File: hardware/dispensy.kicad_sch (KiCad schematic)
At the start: 16 parts, among them U1 DBT50G-7_62-4P, U2 USB-A

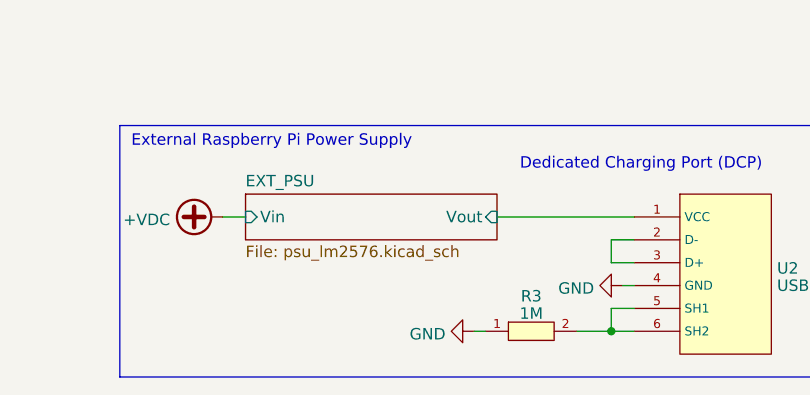
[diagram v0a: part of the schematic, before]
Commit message: add screw connector for 5v-ext
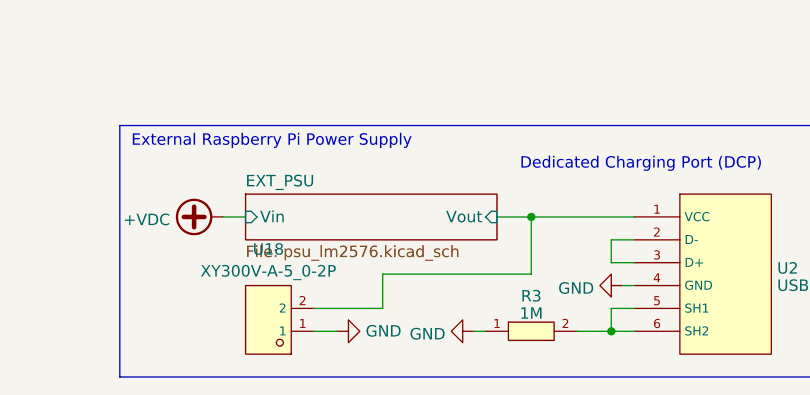
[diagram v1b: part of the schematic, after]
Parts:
- added U18: XY300V-A-5_0-2P, jlc_footprints:CONN-TH_XY300V-A-5.0-2P, symbol jlc:XY300V-A-5_0-2P
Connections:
- net EXT_PSU/Vout: now also U18.2
- net GND: now also U18.1
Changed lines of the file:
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@@
   (title_block
     (title "Dispensy Mainboard")
-    (date "2024-01-20")
+    (date "2024-01-21")
     (rev "0")
     (company "DrinkRobotics")
@@
     (comment 4 "Copyright (c) 2023 - 2024 Thomas Buck <thomas@xythobuz.de>")
   )
+  (junction (at 134.62 173.99) (diameter 0) (color 0 0 0 0)
+  )
   (junction (at 44.45 172.72) (diameter 0) (color 0 0 0 0)
   )
@@
   (junction (at 105.41 44.45) (diameter 0) (color 0 0 0 0)
   )
+  (wire (pts (xy 110.49 184.15) (xy 118.11 184.15))
+    (stroke (width 0) (type default))
+  )
   (wire (pts (xy 143.51 186.69) (xy 139.7 186.69))
     (stroke (width 0) (type default))
@@
     (stroke (width 0) (type default))
   )
+  (wire (pts (xy 118.11 180.34) (xy 134.62 180.34))
+    (stroke (width 0) (type default))
+  )
   (wire (pts (xy 90.17 78.74) (xy 101.6 78.74))
     (stroke (width 0) (type default))
@@
     (stroke (width 0) (type default))
   )
+  (wire (pts (xy 110.49 186.69) (xy 113.03 186.69))
+    (stroke (width 0) (type default))
+  )
   (wire (pts (xy 88.9 132.08) (xy 90.17 132.08))
     (stroke (width 0) (type default))
@@
     (stroke (width 0) (type default))
   )
+  (wire (pts (xy 134.62 180.34) (xy 134.62 173.99))
+    (stroke (width 0) (type default))
+  )
   (wire (pts (xy 99.06 76.2) (xy 99.06 69.85))
     (stroke (width 0) (type default))
@@
     (stroke (width 0) (type default))
   )
+  (wire (pts (xy 134.62 173.99) (xy 146.05 173.99))
+    (stroke (width 0) (type default))
+  )
   (wire (pts (xy 46.99 175.26) (xy 44.45 175.26))
     (stroke (width 0) (type default))
@@
     (stroke (width 0) (type default))
   )
-  (wire (pts (xy 130.81 173.99) (xy 146.05 173.99))
+  (wire (pts (xy 130.81 173.99) (xy 134.62 173.99))
     (stroke (width 0) (type default))
   )
@@
   )
   (wire (pts (xy 74.93 100.33) (xy 74.93 57.15))
+    (stroke (width 0) (type default))
+  )
+  (wire (pts (xy 118.11 184.15) (xy 118.11 180.34))
     (stroke (width 0) (type default))
   )
@@
     )
   )
+  (symbol (lib_id "jlc:XY300V-A-5_0-2P") (at 105.41 185.42 180) (unit 1)
+    (in_bom yes) (on_board yes) (dnp no) (fields_autoplaced)
+    (property "Reference" "U18" (at 105.41 177.5927 0)
+      (effects (font (size 1.27 1.27)))
+    )
+    (property "Value" "XY300V-A-5_0-2P" (at 105.41 180.0169 0)
+      (effects (font (size 1.27 1.27)))
+    )
+    (property "Footprint" "jlc_footprints:CONN-TH_XY300V-A-5.0-2P" (at 105.41 175.26 0)
+      (effects (font (size 1.27 1.27) italic) hide)
+    )
+    (property "Datasheet" "https://atta.szlcsc.com/upload/public/pdf/source/20200527/C557648_4A2FA4132AA24EE423B62B1474E9B5BB.pdf" (at 107.696 185.547 0)
+      (effects (font (size 1.27 1.27)) (justify left) hide)
+    )
+    (property "LCSC" "C557648" (at 105.41 185.42 0)
+      (effects (font (size 1.27 1.27)) hide)
+    )
+    (pin "2")
+    (pin "1")
+    (instances
+      (project "dispensy"
+        (path "/a50b51f9-900f-4bbb-8934-4acbc429c37b"
+          (reference "U18") (unit 1)
+        )
+      )
+    )
+  )
   (symbol (lib_id "jlc:CR-02FL6---10K") (at 95.25 107.95 0) (unit 1)
     (in_bom yes) (on_board yes) (dnp no) (fields_autoplaced)
@@
         )
       )
+    )
+  )
+  (symbol (lib_id "power:GND") (at 113.03 186.69 90) (unit 1)
+    (in_bom yes) (on_board yes) (dnp no) (fields_autoplaced)
+    (property "Reference" "#PWR073" (at 119.38 186.69 0)
+      (effects (font (size 1.27 1.27)) hide)
+    )
+    (property "Value" "GND" (at 116.205 186.69 90)
+      (effects (font (size 1.27 1.27)) (justify right))
+    )
+    (property "Footprint" "" (at 113.03 186.69 0)
+      (effects (font (size 1.27 1.27)) hide)
+    )
+    (property "Datasheet" "" (at 113.03 186.69 0)
+      (effects (font (size 1.27 1.27)) hide)
+    )
+    (pin "1")
+    (instances
+      (project "dispensy"
+        (path "/a50b51f9-900f-4bbb-8934-4acbc429c37b"
+          (reference "#PWR073") (unit 1)
+        )
+      )

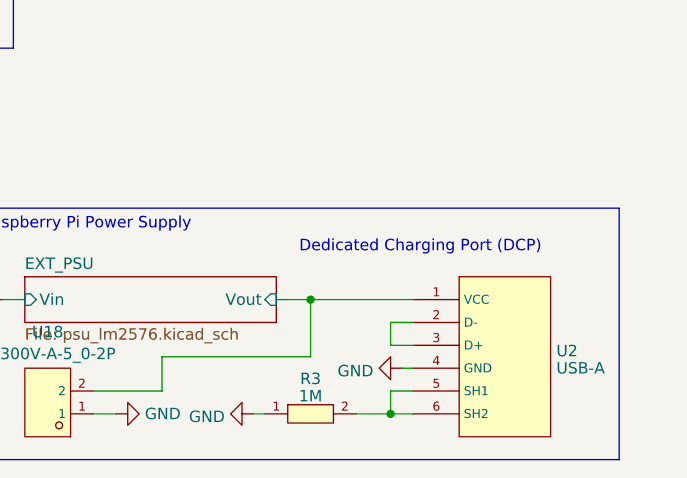
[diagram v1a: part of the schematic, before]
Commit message: add resettable fuse to 5v ext output
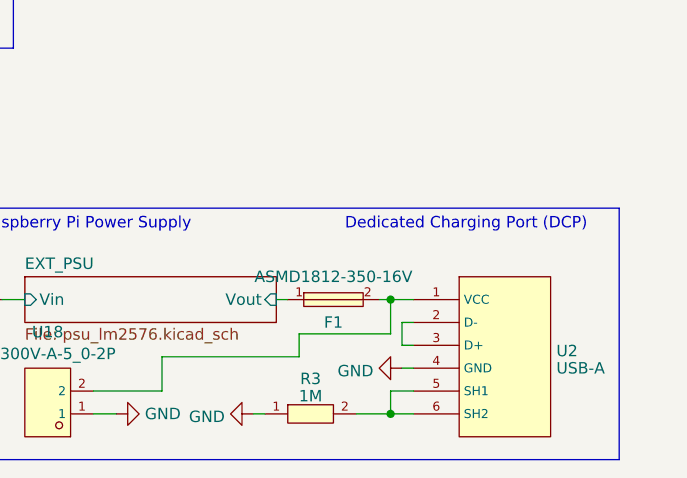
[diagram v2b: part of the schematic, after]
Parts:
- added F1: ASMD1812-350-16V, jlc_footprints:F1812, symbol jlc:ASMD1812-350-16V
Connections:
- net EXT_PSU/Vout: now also F1.1; no longer U18.2, U2.1 (VCC)
- new net: F1.2, U18.2, U2.1 (VCC)
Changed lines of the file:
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@@
     (comment 4 "Copyright (c) 2023 - 2024 Thomas Buck <thomas@xythobuz.de>")
   )
-  (junction (at 134.62 173.99) (diameter 0) (color 0 0 0 0)
-  )
   (junction (at 44.45 172.72) (diameter 0) (color 0 0 0 0)
   )
@@
   (junction (at 105.41 44.45) (diameter 0) (color 0 0 0 0)
   )
+  (junction (at 143.51 173.99) (diameter 0) (color 0 0 0 0)
+  )
   (wire (pts (xy 110.49 184.15) (xy 118.11 184.15))
     (stroke (width 0) (type default))
   )
+  (wire (pts (xy 133.35 177.8) (xy 143.51 177.8))
+    (stroke (width 0) (type default))
+  )
   (wire (pts (xy 143.51 186.69) (xy 139.7 186.69))
     (stroke (width 0) (type default))
   )
-  (wire (pts (xy 143.51 176.53) (xy 146.05 176.53))
+  (wire (pts (xy 144.78 176.53) (xy 146.05 176.53))
     (stroke (width 0) (type default))
   )
@@
     (stroke (width 0) (type default))
   )
+  (wire (pts (xy 133.35 180.34) (xy 133.35 177.8))
+    (stroke (width 0) (type default))
+  )
   (wire (pts (xy 101.6 78.74) (xy 101.6 72.39))
     (stroke (width 0) (type default))
@@
     (stroke (width 0) (type default))
   )
-  (wire (pts (xy 118.11 180.34) (xy 134.62 180.34))
+  (wire (pts (xy 118.11 180.34) (xy 133.35 180.34))
     (stroke (width 0) (type default))
   )
@@
     (stroke (width 0) (type default))
   )
+  (wire (pts (xy 142.24 173.99) (xy 143.51 173.99))
+    (stroke (width 0) (type default))
+  )
   (wire (pts (xy 147.32 38.1) (xy 147.32 49.53))
     (stroke (width 0) (type default))
@@
     (stroke (width 0) (type default))
   )
-  (wire (pts (xy 134.62 180.34) (xy 134.62 173.99))
-    (stroke (width 0) (type default))
-  )
   (wire (pts (xy 99.06 76.2) (xy 99.06 69.85))
     (stroke (width 0) (type default))
@@
     (stroke (width 0) (type default))
   )
+  (wire (pts (xy 143.51 173.99) (xy 146.05 173.99))
+    (stroke (width 0) (type default))
+  )
   (wire (pts (xy 74.93 135.89) (xy 74.93 100.33))
     (stroke (width 0) (type default))
@@
     (stroke (width 0) (type default))
   )
-  (wire (pts (xy 146.05 179.07) (xy 143.51 179.07))
+  (wire (pts (xy 146.05 179.07) (xy 144.78 179.07))
     (stroke (width 0) (type default))
   )
@@
     (stroke (width 0) (type default))
   )
+  (wire (pts (xy 130.81 173.99) (xy 132.08 173.99))
+    (stroke (width 0) (type default))
+  )
   (wire (pts (xy 142.24 44.45) (xy 127 44.45))
     (stroke (width 0) (type default))
@@
     (stroke (width 0) (type default))
   )
-  (wire (pts (xy 134.62 173.99) (xy 146.05 173.99))
-    (stroke (width 0) (type default))
-  )
   (wire (pts (xy 46.99 175.26) (xy 44.45 175.26))
     (stroke (width 0) (type default))
   )
+  (wire (pts (xy 143.51 177.8) (xy 143.51 173.99))
+    (stroke (width 0) (type default))
+  )
   (wire (pts (xy 165.1 115.57) (xy 137.16 115.57))
     (stroke (width 0) (type default))
@@
     (stroke (width 0) (type default))
   )
-  (wire (pts (xy 130.81 173.99) (xy 134.62 173.99))
-    (stroke (width 0) (type default))
-  )
   (wire (pts (xy 163.83 57.15) (xy 163.83 55.88))
     (stroke (width 0) (type default))
@@
     (stroke (width 0) (type default))
   )
-  (wire (pts (xy 143.51 179.07) (xy 143.51 176.53))
+  (wire (pts (xy 144.78 179.07) (xy 144.78 176.53))
     (stroke (width 0) (type default))
   )
@@
     (effects (font (size 1.27 1.27)) (justify left top))
   )
-  (text "Dedicated Charging Port (DCP)" (at 133.35 168.91 0)
+  (text "Dedicated Charging Port (DCP)" (at 138.43 166.37 0)
     (effects (font (size 1.27 1.27)) (justify left bottom) (href "https://electronics.stackexchange.com/a/200581"))
   )
@@
         )
       )
+    )
+  )
+  (symbol (lib_id "jlc:ASMD1812-350-16V") (at 137.16 173.99 0) (unit 1)
+    (in_bom yes) (on_board yes) (dnp no)
+    (property "Reference" "F1" (at 137.16 176.53 0)
+      (effects (font (size 1.27 1.27)))
+    )
+    (property "Value" "ASMD1812-350-16V" (at 137.16 171.45 0)
+      (effects (font (size 1.27 1.27)))
+    )
+    (property "Footprint" "jlc_footprints:F1812" (at 137.16 184.15 0)
+      (effects (font (size 1.27 1.27) italic) hide)
+    )
+    (property "Datasheet" "https://item.szlcsc.com/343302.html" (at 134.874 173.863 0)
+      (effects (font (size 1.27 1.27)) (justify left) hide)
+    )
+    (property "LCSC" "C2982285" (at 137.16 173.99 0)
+      (effects (font (size 1.27 1.27)) hide)
+    )
+    (pin "1")
+    (pin "2")
+    (instances
+      (project "dispensy"
+        (path "/a50b51f9-900f-4bbb-8934-4acbc429c37b"
+          (reference "F1") (unit 1)
+        )
+      )

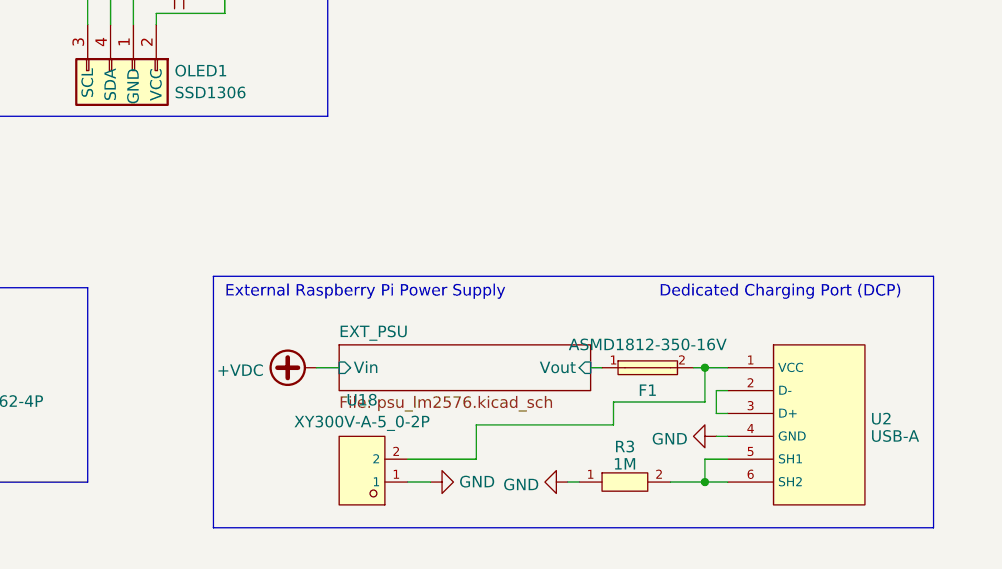
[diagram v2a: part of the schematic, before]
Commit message: add power status leds
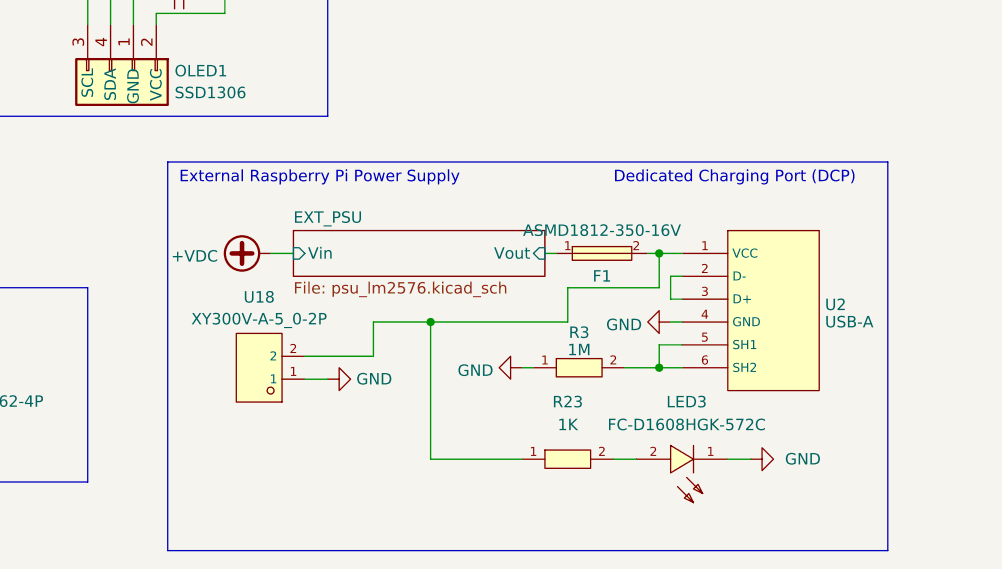
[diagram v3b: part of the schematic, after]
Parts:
- added LED3: FC-D1608HGK-572C, jlc_footprints:LED0603-RD, symbol jlc:FC-D1608HGK-572C
- added R23: 1K, jlc_footprints:R0402, symbol jlc:CR-02FL6----1K
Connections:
- net GND: now also LED3.1 (-)
- net at F1.2, U18.2, U2.1 (VCC): now also R23.1
- new net: LED3.2 (+), R23.2
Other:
- moved on the sheet: F1, R3, U18, U2

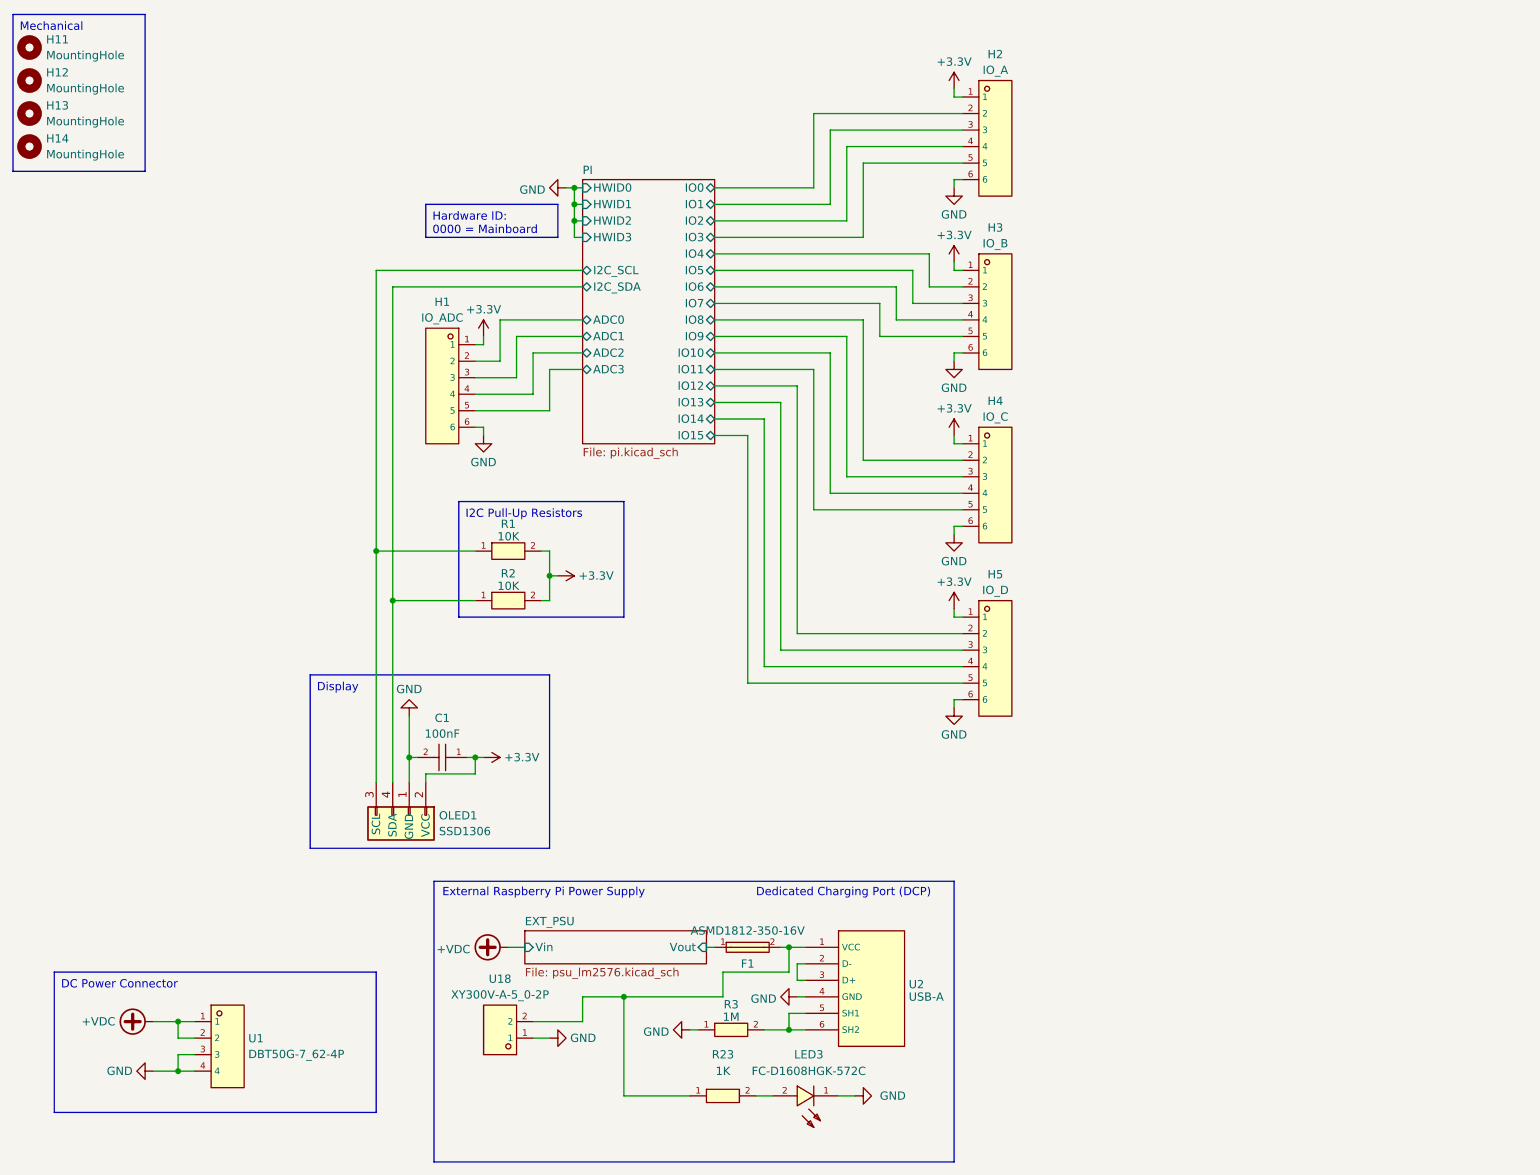
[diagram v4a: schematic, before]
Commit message: add resistive divider for power in measurement. add buttons for display. remove gpio headers.
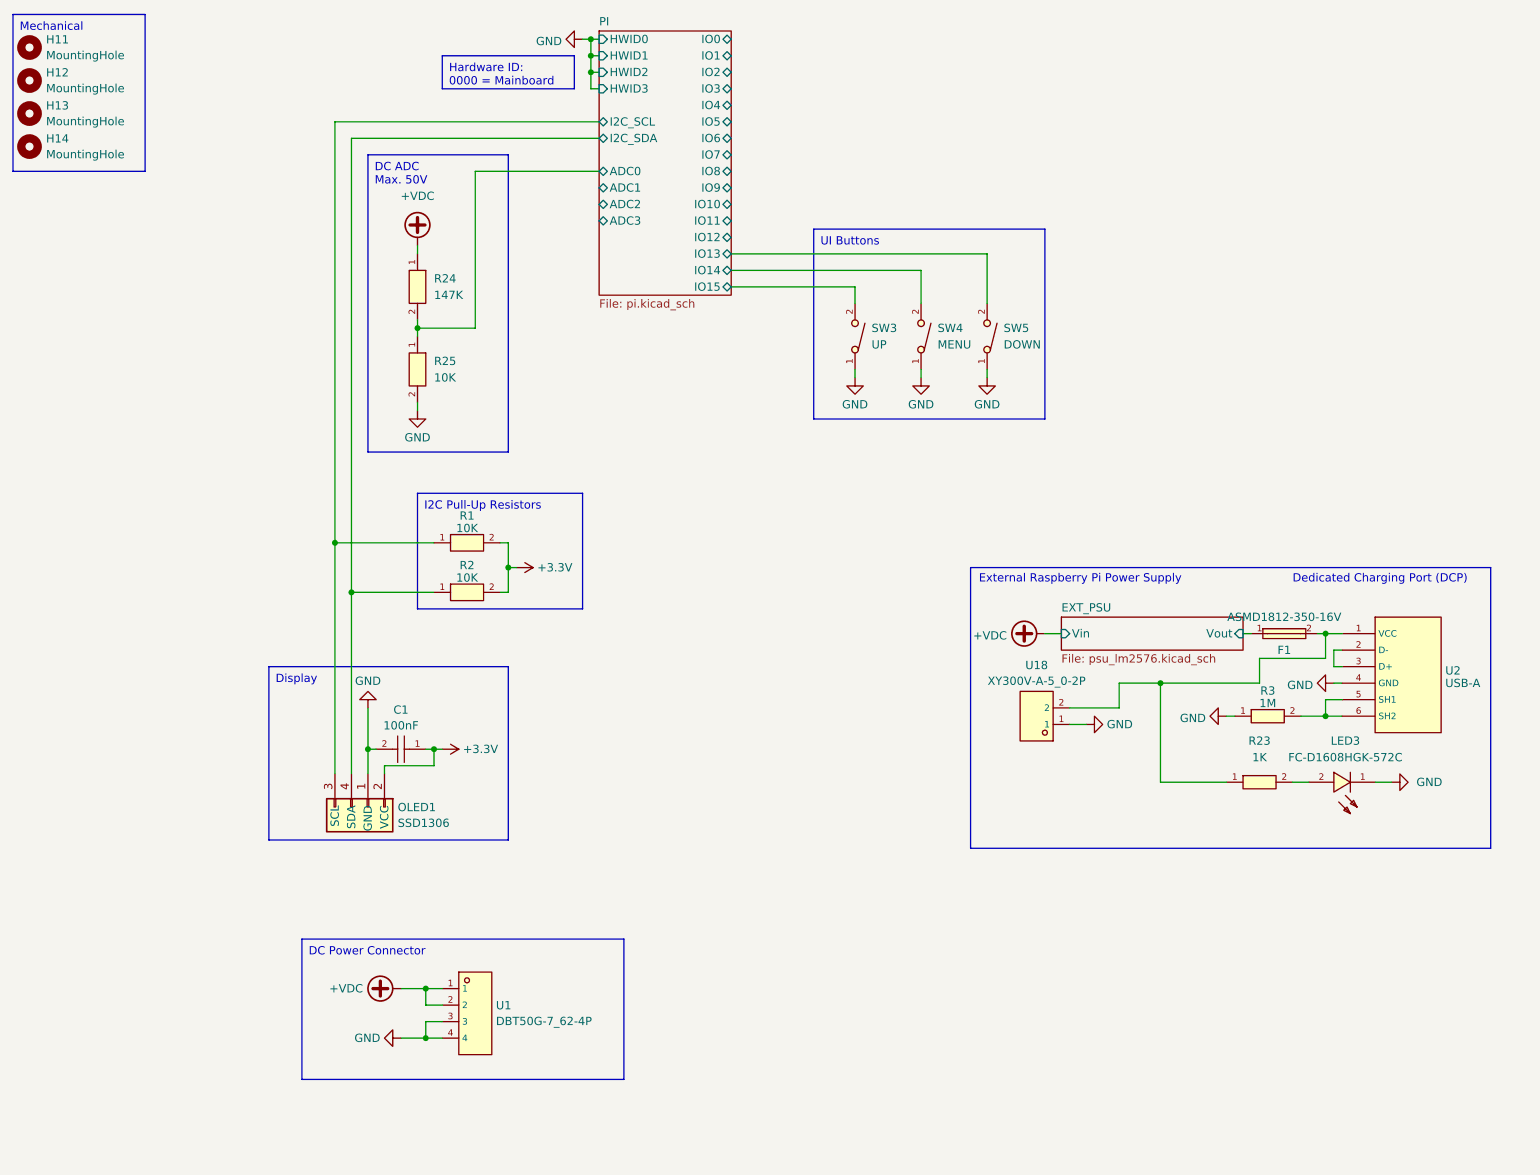
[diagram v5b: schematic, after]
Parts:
- removed H1: IO_ADC, jlc_footprints:HDR-TH_6P-P2.54-V-F, symbol jlc:Header-Female-2_54_1x6
- removed H2: IO_A, jlc_footprints:HDR-TH_6P-P2.54-V-F, symbol jlc:Header-Female-2_54_1x6
- removed H3: IO_B, jlc_footprints:HDR-TH_6P-P2.54-V-F, symbol jlc:Header-Female-2_54_1x6
- removed H4: IO_C, jlc_footprints:HDR-TH_6P-P2.54-V-F, symbol jlc:Header-Female-2_54_1x6
- removed H5: IO_D, jlc_footprints:HDR-TH_6P-P2.54-V-F, symbol jlc:Header-Female-2_54_1x6
- added R24: 147K, jlc_footprints:R0402, symbol jlc:CR0402F147KQ10Z
- added R25: 10K, jlc_footprints:R0402, symbol jlc:CR-02FL6---10K
- added SW3: UP, jlc_footprints:SW-SMD_L6.1-W3.6-LS6.6, symbol jlc:TS-1092U-B3D2
- added SW4: MENU, jlc_footprints:SW-SMD_L6.1-W3.6-LS6.6, symbol jlc:TS-1092U-B3D2
- added SW5: DOWN, jlc_footprints:SW-SMD_L6.1-W3.6-LS6.6, symbol jlc:TS-1092U-B3D2
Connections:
- net +VDC: now also R24.1
- net GND: now also R25.2, SW3.1, SW4.1, SW5.1
- net PI/ADC0: now also R24.2, R25.1
- net PI/IO13: now also SW5.2
- net PI/IO14: now also SW4.2
- net PI/IO15: now also SW3.2
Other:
- moved on the sheet: C1, F1, LED3, OLED1, R1, R2, R23, R3, U1, U18, U2
